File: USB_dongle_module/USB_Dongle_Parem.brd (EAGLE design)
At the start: 43.6 x 20 mm, 29 parts, among them IC3 FT230XS, X1 USB-A

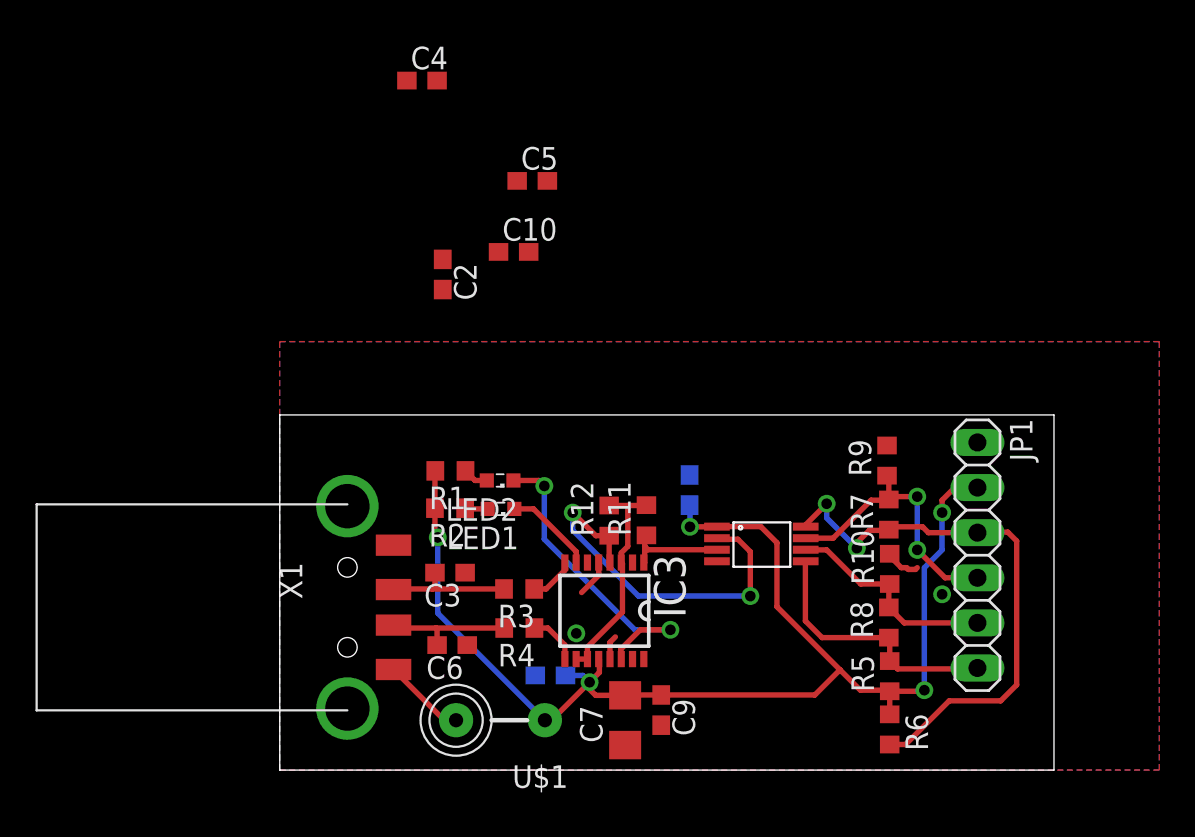
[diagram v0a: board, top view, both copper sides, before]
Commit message: Korrastasin boardi
Tegin mõned muudatused skeemis ning korrastasin boardi. Valmis!
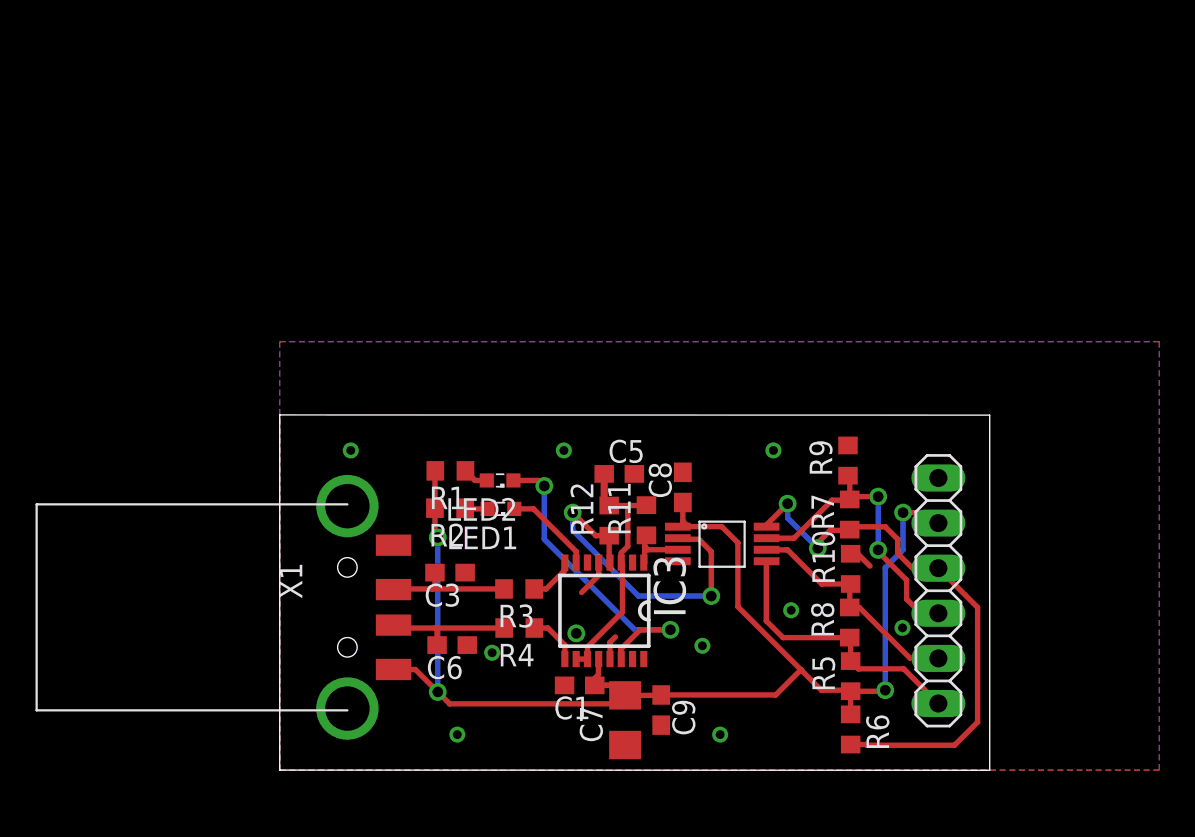
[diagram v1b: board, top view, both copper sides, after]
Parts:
- removed C10, C4: 100n, eagle-ltspice:C0603
- removed C2: 10n, eagle-ltspice:C0603
- removed U$1: FB, adafruit:FB
- moved C5 17.2 mm to (19.1, 16.7)
- moved JP1 2.97 mm to (37.1, 10.1)
- moved R10 2.20 mm to (32.1, 11.3)
- moved R5 2.20 mm to (32.1, 5.29)
- moved R6 2.20 mm to (32.1, 2.29)
- moved R9 2.20 mm to (32.0, 17.4)
- moved U$2 2.20 mm to (24.9, 12.7)
- moved R7 2.20 mm to (32.1, 14.4)
- moved R8 2.20 mm to (32.1, 8.31)
- moved C1 1.74 mm to (16.9, 4.77), flipped to the top, turned to 180 degrees
- moved C8 0.41 mm to (22.7, 15.9), flipped to the top
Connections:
- removed net N$6: C2.1, U$1.P$2, X1.1
- net GND: no longer C10.1, C2.2, C4.2
- net VCC: now also X1.1; no longer C10.2, C4.1, U$1.P$1
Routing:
- net N$6: track 4.70 -> 0.00 mm
- net VCC: track 73.4 -> 75.9 mm, vias 5 -> 4
- net TXD: track 5.77 -> 3.57 mm
- net RXD: track 21.4 -> 19.2 mm
- net VCCIO: track 12.4 -> 14.4 mm
- net B: track 15.7 -> 17.2 mm
- net Z: track 12.2 -> 13.0 mm
- net Y: track 14.9 -> 15.7 mm
- net GND: track 5.53 -> 4.87 mm, vias 2 -> 10
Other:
- board size 43.6 x 20 mm -> 40 x 20 mm

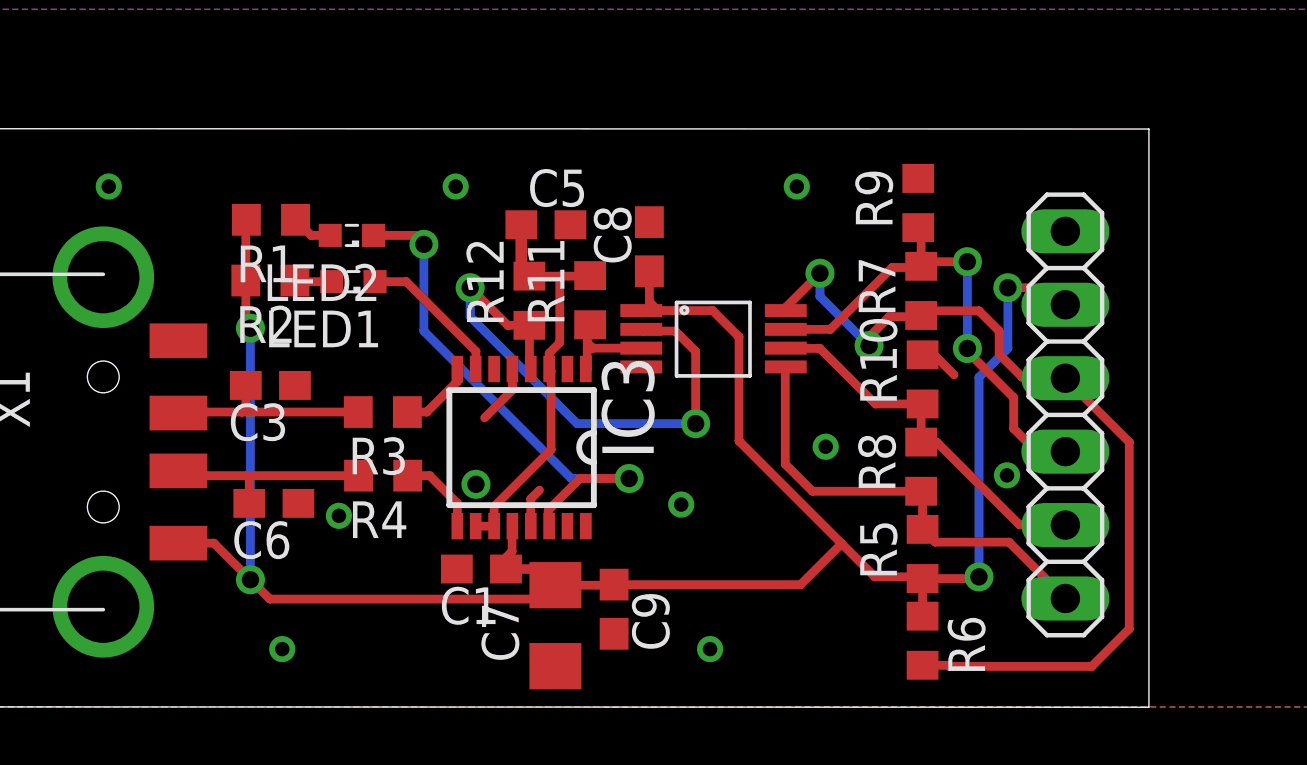
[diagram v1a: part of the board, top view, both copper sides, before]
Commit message: Pinheader>Micromatch
Vahetasin siis komponendi välja, lisaks muutsin kondekate asukohta.
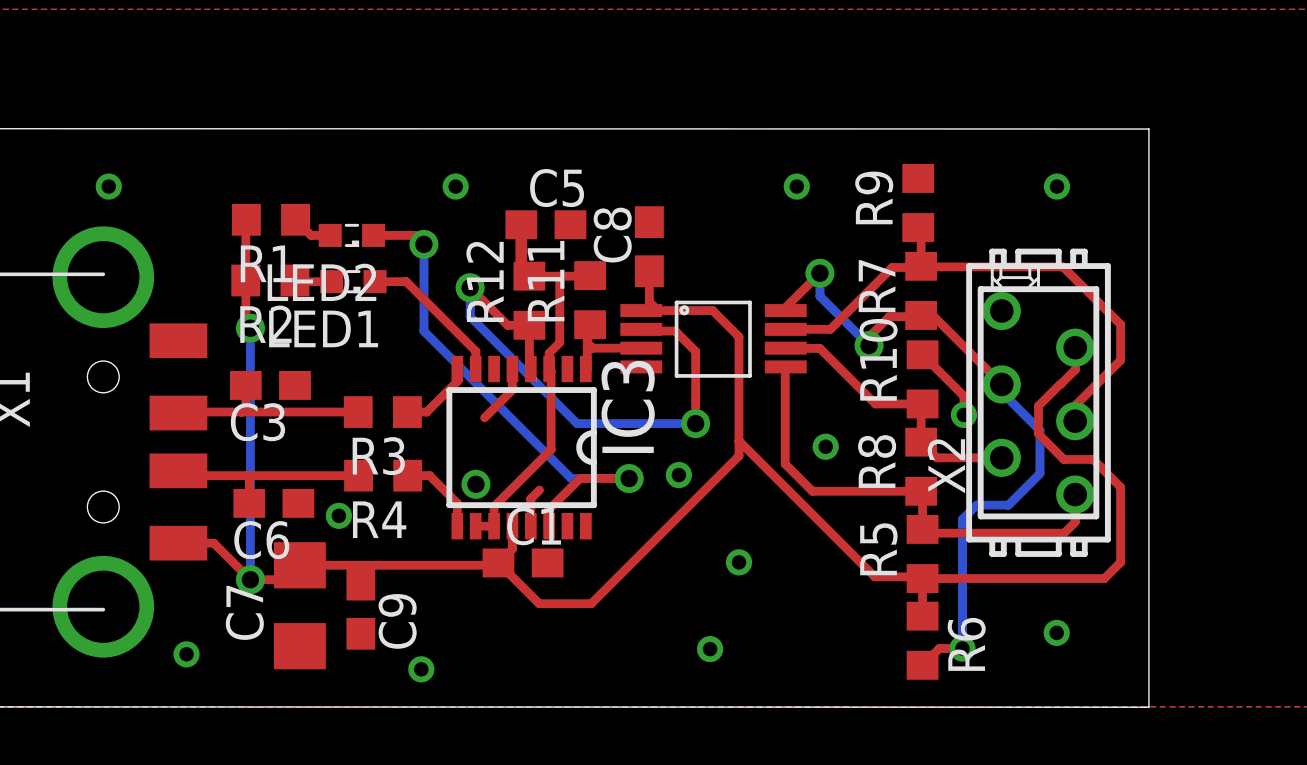
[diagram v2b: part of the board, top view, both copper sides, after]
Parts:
- removed JP1: (no value), pinhead:1X06
- added X2: MICROMATCH-6, con-amp-micromatch:MICROMATCH-6
- moved C7 8.87 mm to (10.6, 3.50)
- moved C9 8.76 mm to (12.7, 3.38)
- moved C1 1.46 mm to (18.3, 4.98), turned to 0 degrees
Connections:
- net A: now also X2.3; no longer JP1.3
- net B: now also X2.4; no longer JP1.4
- net GND: now also X2.1; no longer JP1.1
- net VCC: now also X2.2; no longer JP1.2
- net Y: now also X2.6; no longer JP1.6
- net Z: now also X2.5; no longer JP1.5
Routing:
- net A: track 31.2 -> 24.4 mm, vias 2 -> 3
- net VCC: track 75.9 -> 72.7 mm, vias 4 -> 2
- net Z: track 13.0 -> 9.89 mm
- net B: track 17.2 -> 19.4 mm, vias 2 -> 0
- net GND: track 4.87 -> 6.17 mm, vias 10 -> 14
- net Y: track 15.7 -> 16.2 mm

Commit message: Minor fixes
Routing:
- net VCC: track 72.7 -> 73.5 mm
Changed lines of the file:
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@@
 <?xml version="1.0" encoding="utf-8"?>
 <!DOCTYPE eagle SYSTEM "eagle.dtd">
-<eagle version="6.5.0">
+<eagle version="7.3.0">
 <drawing>
 <settings>
@@
 <layer number="43" name="vRestrict" color="2" fill="10" visible="yes" active="yes"/>
 <layer number="44" name="Drills" color="7" fill="1" visible="no" active="yes"/>
-<layer number="45" name="Holes" color="7" fill="1" visible="no" active="yes"/>
+<layer number="45" name="Holes" color="7" fill="1" visible="yes" active="yes"/>
 <layer number="46" name="Milling" color="3" fill="1" visible="no" active="yes"/>
 <layer number="47" name="Measures" color="7" fill="1" visible="no" active="yes"/>
@@
 <dimension x1="0" y1="20" x2="40" y2="20" x3="20" y3="22" textsize="1.778" layer="51"/>
 <dimension x1="39.98" y1="19.99" x2="39.98" y2="-0.01" x3="42" y3="9.99" textsize="1.778" layer="51"/>
+<hole x="36.64" y="15.55" drill="1.2"/>
 </plain>
 <attributes>
@@
 <pass name="Default">
 <param name="RoutingGrid" value="50mil"/>
+<param name="AutoGrid" value="1"/>
+<param name="Efforts" value="0"/>
+<param name="TopRouterVariant" value="1"/>
 <param name="tpViaShape" value="round"/>
 <param name="PrefDir.1" value="|"/>
@@
 <contactref element="R5" pad="1"/>
 <contactref element="U$2" pad="1"/>
-<wire x1="32.15" y1="3.14" x2="32.15" y2="4.44" width="0.3048" layer="1"/>
-<wire x1="22.42" y1="13.71" x2="23" y2="13.71" width="0.3048" layer="1"/>
-<wire x1="23" y1="13.71" x2="24.89" y2="13.71" width="0.3048" layer="1"/>
-<wire x1="24.89" y1="13.71" x2="25.8" y2="12.8" width="0.3048" layer="1"/>
-<wire x1="25.8" y1="12.8" x2="25.8" y2="9.2" width="0.3048" layer="1"/>
-<wire x1="25.8" y1="9.2" x2="30.5" y2="4.5" width="0.3048" layer="1"/>
-<wire x1="30.5" y1="4.5" x2="32.09" y2="4.5" width="0.3048" layer="1"/>
+<wire x1="32.15" y1="3.14" x2="32.15" y2="4.44" width="0.4064" layer="1"/>
+<wire x1="24.89" y1="13.71" x2="25.8" y2="12.8" width="0.4064" layer="1"/>
+<wire x1="25.8" y1="12.8" x2="25.8" y2="8.68" width="0.4064" layer="1"/>
 <wire x1="32.09" y1="4.5" x2="32.15" y2="4.44" width="0.3048" layer="1"/>
-<wire x1="8.74" y1="14.75" x2="8.74" y2="13.26" width="0.3048" layer="1"/>
+<wire x1="8.74" y1="14.75" x2="8.74" y2="13.26" width="0.4064" layer="1"/>
 <wire x1="8.74" y1="13.26" x2="8.9" y2="13.1" width="0.3048" layer="1"/>
 <via x="8.9" y="13.1" extent="1-16" drill="0.6"/>
-<wire x1="8.74" y1="14.75" x2="8.74" y2="16.83" width="0.3048" layer="1"/>
+<wire x1="8.74" y1="14.75" x2="8.74" y2="16.83" width="0.4064" layer="1"/>
 <wire x1="8.74" y1="16.83" x2="8.76" y2="16.85" width="0.3048" layer="1"/>
 <contactref element="X1" pad="1"/>
-<wire x1="6.41" y1="5.665" x2="7.635" y2="5.665" width="0.3048" layer="1"/>
-<wire x1="7.635" y1="5.665" x2="8.9" y2="4.4" width="0.3048" layer="1"/>
 <via x="8.9" y="4.4" extent="1-16" drill="0.6"/>
-<wire x1="8.9" y1="4.4" x2="8.9" y2="13.1" width="0.3048" layer="16"/>
+<wire x1="8.9" y1="4.4" x2="8.9" y2="13.1" width="0.4064" layer="16"/>
 <contactref element="C7" pad="2"/>
-<wire x1="22.7" y1="15.07" x2="22.7" y2="14.01" width="0.3048" layer="1"/>
-<wire x1="22.7" y1="14.01" x2="23" y2="13.71" width="0.3048" layer="1"/>
 <contactref element="X2" pad="2"/>
-<wire x1="32.15" y1="4.44" x2="38.44" y2="4.44" width="0.3048" layer="1"/>
-<wire x1="38.44" y1="4.44" x2="39" y2="5" width="0.3048" layer="1"/>
-<wire x1="39" y1="5" x2="39" y2="7.6" width="0.3048" layer="1"/>
-<wire x1="39" y1="7.6" x2="38.32" y2="8.28" width="0.3048" layer="1"/>
-<wire x1="38.32" y1="8.28" x2="38.32" y2="8.29" width="0.3048" layer="1"/>
-<wire x1="38.32" y1="8.29" x2="38.05" y2="8.56" width="0.3048" layer="1"/>
-<wire x1="38.05" y1="8.56" x2="37.04" y2="8.56" width="0.3048" layer="1"/>
-<wire x1="37.04" y1="8.56" x2="36.16" y2="9.44" width="0.3048" layer="1"/>
-<wire x1="36.16" y1="9.44" x2="36.16" y2="10.41" width="0.3048" layer="1"/>
-<wire x1="36.16" y1="10.41" x2="36.91" y2="11.16" width="0.3048" layer="1"/>
+<wire x1="32.15" y1="4.44" x2="38.44" y2="4.44" width="0.4064" layer="1"/>
+<wire x1="38.44" y1="4.44" x2="39" y2="5" width="0.4064" layer="1"/>
+<wire x1="39" y1="5" x2="39" y2="7.61" width="0.4064" layer="1"/>
+<wire x1="38.05" y1="8.56" x2="37.04" y2="8.56" width="0.4064" layer="1"/>
+<wire x1="37.04" y1="8.56" x2="36.16" y2="9.44" width="0.4064" layer="1"/>
+<wire x1="36.16" y1="9.44" x2="36.16" y2="10.41" width="0.4064" layer="1"/>
+<wire x1="36.16" y1="10.41" x2="36.91" y2="11.16" width="0.4064" layer="1"/>
 <wire x1="36.91" y1="11.16" x2="36.93" y2="11.16" width="0.3048" layer="1"/>
-<wire x1="36.93" y1="11.16" x2="37.44" y2="11.67" width="0.3048" layer="1"/>
-<wire x1="37.44" y1="11.67" x2="37.44" y2="12.415" width="0.3048" layer="1"/>
+<wire x1="36.93" y1="11.16" x2="37.44" y2="11.67" width="0.4064" layer="1"/>
+<wire x1="37.44" y1="11.67" x2="37.44" y2="12.415" width="0.4064" layer="1"/>
 <wire x1="37.44" y1="12.415" x2="37.43" y2="12.425" width="0.3048" layer="1"/>
-<wire x1="8.9" y1="4.4" x2="10.26" y2="4.4" width="0.3048" layer="1"/>
 <wire x1="17.9625" y1="6.2522" x2="17.9625" y2="5.4625" width="0.3048" layer="1"/>
 <wire x1="17.9625" y1="5.4625" x2="17.48" y2="4.98" width="0.3048" layer="1"/>
-<wire x1="25.8" y1="9.2" x2="25.8" y2="8.68" width="0.3048" layer="1"/>
-<wire x1="25.8" y1="8.68" x2="20.69" y2="3.57" width="0.3048" layer="1"/>
-<wire x1="20.69" y1="3.57" x2="18.89" y2="3.57" width="0.3048" layer="1"/>
-<wire x1="18.89" y1="3.57" x2="17.48" y2="4.98" width="0.3048" layer="1"/>
+<wire x1="25.8" y1="8.68" x2="20.69" y2="3.57" width="0.4064" layer="1"/>
+<wire x1="20.69" y1="3.57" x2="18.89" y2="3.57" width="0.4064" layer="1"/>
+<wire x1="18.89" y1="3.57" x2="17.48" y2="4.98" width="0.4064" layer="1"/>
 <wire x1="10.26" y1="4.4" x2="10.26" y2="4.55" width="0.3048" layer="1"/>
 <wire x1="10.26" y1="4.55" x2="10.61" y2="4.9" width="0.3048" layer="1"/>
-<wire x1="10.61" y1="4.9" x2="17.4" y2="4.9" width="0.3048" layer="1"/>
 <wire x1="17.4" y1="4.9" x2="17.48" y2="4.98" width="0.3048" layer="1"/>
-<wire x1="10.61" y1="4.9" x2="12.72" y2="4.23" width="0" layer="19" extent="1-1"/>
+<wire x1="6.41" y1="5.665" x2="6.425" y2="5.68" width="0.4064" layer="1"/>
+<wire x1="6.425" y1="5.68" x2="7.66" y2="5.68" width="0.4064" layer="1"/>
+<wire x1="7.66" y1="5.68" x2="8.9" y2="4.44" width="0.4064" layer="1"/>
+<wire x1="8.9" y1="4.44" x2="8.9" y2="4.4" width="0.4064" layer="1"/>
+<wire x1="8.9" y1="4.44" x2="9.01" y2="4.55" width="0.4064" layer="1"/>
+<wire x1="9.01" y1="4.55" x2="10.26" y2="4.55" width="0.4064" layer="1"/>
+<wire x1="10.61" y1="4.9" x2="10.69" y2="4.98" width="0.4064" layer="1"/>
+<wire x1="12.75" y1="4.98" x2="17.48" y2="4.98" width="0.4064" layer="1"/>
+<wire x1="10.69" y1="4.98" x2="12.75" y2="4.98" width="0.4064" layer="1"/>
+<wire x1="12.75" y1="4.98" x2="12.72" y2="4.95" width="0.4064" layer="1"/>
+<wire x1="12.72" y1="4.95" x2="12.72" y2="4.23" width="0.4064" layer="1"/>
+<wire x1="32.09" y1="4.5" x2="29.98" y2="4.5" width="0.4064" layer="1"/>
+<wire x1="29.98" y1="4.5" x2="25.8" y2="8.68" width="0.4064" layer="1"/>
+<wire x1="39" y1="7.61" x2="38.05" y2="8.56" width="0.4064" layer="1"/>
+<wire x1="24.89" y1="13.71" x2="23.38" y2="13.71" width="0.4064" layer="1"/>
+<wire x1="23.38" y1="13.71" x2="22.42" y2="13.71" width="0.3048" layer="1"/>
+<wire x1="22.7" y1="15.07" x2="22.7" y2="14.14" width="0.4064" layer="1"/>
+<wire x1="22.7" y1="14.14" x2="22.71" y2="14.13" width="0.4064" layer="1"/>
+<wire x1="22.71" y1="14.13" x2="22.71" y2="14" width="0.3048" layer="1"/>
+<wire x1="22.71" y1="14" x2="22.42" y2="13.71" width="0.3048" layer="1"/>
 </signal>
 <signal name="D+">
@@
 <contactref element="LED2" pad="A"/>
 <contactref element="R1" pad="1"/>
-<wire x1="11.66" y1="16.31" x2="11" y2="16.31" width="0.3048" layer="1"/>
-<wire x1="11" y1="16.31" x2="10.46" y2="16.85" width="0.3048" layer="1"/>
+<wire x1="11.66" y1="16.31" x2="11" y2="16.31" width="0.4064" layer="1"/>
+<wire x1="11" y1="16.31" x2="10.46" y2="16.85" width="0.4064" layer="1"/>
 </signal>
 <signal name="N$8">
 <contactref element="LED1" pad="A"/>
 <contactref element="R2" pad="1"/>
-<wire x1="11.71" y1="14.71" x2="10.48" y2="14.71" width="0.3048" layer="1"/>
+<wire x1="11.71" y1="14.71" x2="10.48" y2="14.71" width="0.4064" layer="1"/>
 <wire x1="10.48" y1="14.71" x2="10.44" y2="14.75" width="0.3048" layer="1"/>
 </signal>
@@
 <wire x1="37.43" y1="10.42" x2="39" y2="11.99" width="0.3048" layer="1"/>
 <wire x1="39" y1="11.99" x2="39" y2="13.23" width="0.3048" layer="1"/>
-<wire x1="39" y1="13.23" x2="37.01" y2="15.22" width="0.3048" layer="1"/>
-<wire x1="37.01" y1="15.22" x2="31.61" y2="15.22" width="0.3048" layer="1"/>
 <wire x1="31.61" y1="15.22" x2="31.59" y2="15.2" width="0.3048" layer="1"/>
+<wire x1="39" y1="13.23" x2="38.03" y2="14.2" width="0.3048" layer="1"/>
+<wire x1="32.13" y1="15.21" x2="32.1" y2="15.24" width="0.3048" layer="1"/>
+<wire x1="38.03" y1="14.2" x2="35.99" y2="14.2" width="0.3048" layer="1"/>
+<wire x1="35.99" y1="14.2" x2="34.95" y2="15.24" width="0.3048" layer="1"/>
+<wire x1="34.95" y1="15.24" x2="32.1" y2="15.24" width="0.3048" layer="1"/>
 </signal>
 <signal name="Y">
